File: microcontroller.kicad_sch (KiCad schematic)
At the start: 5 parts, among them CN4 Samtec FTSH-107-01-L-DV-K, CN5 M20-9990346, U2 TMP102AIDRL, U3 Microchip 24AA256UIDT-I/ST, U4 STM32H743VIT6

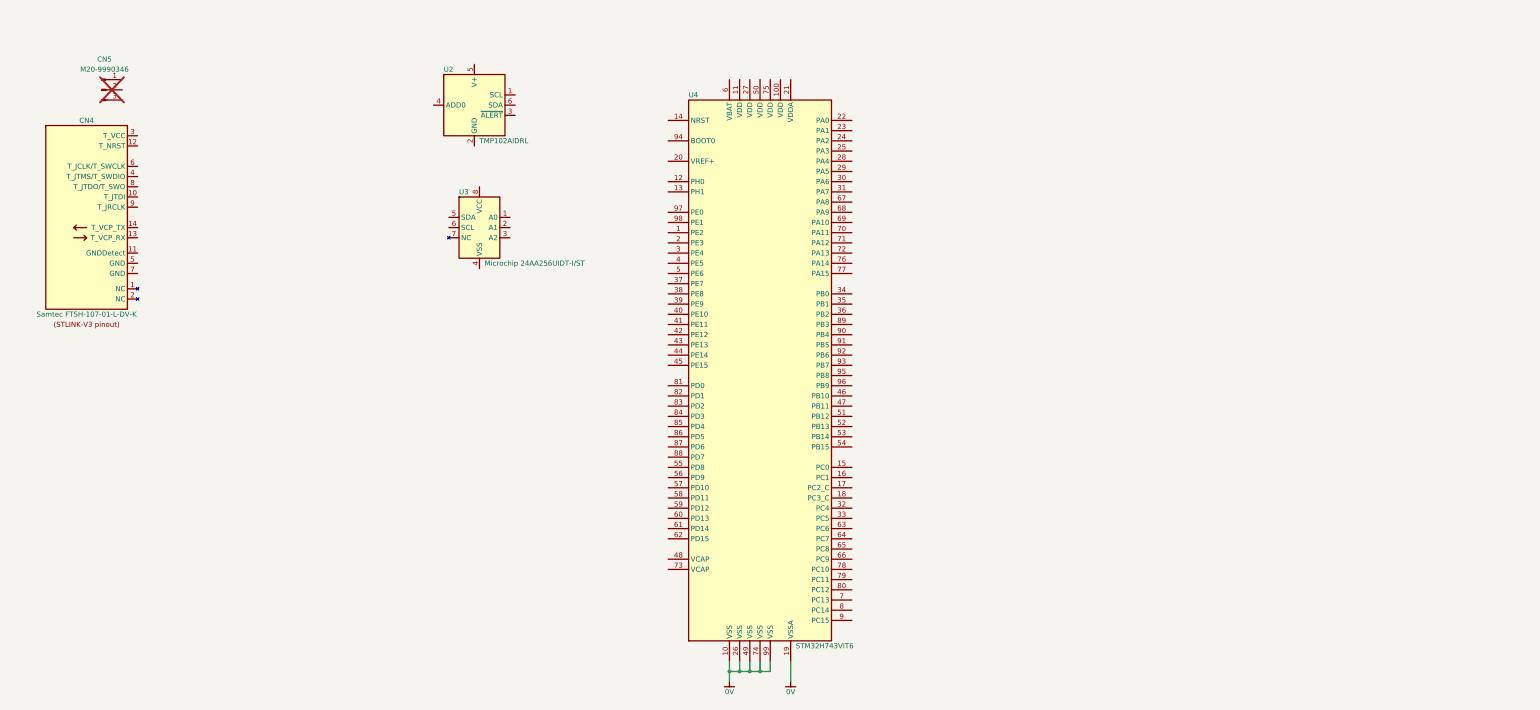
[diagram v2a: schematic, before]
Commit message: started on mcu pinout
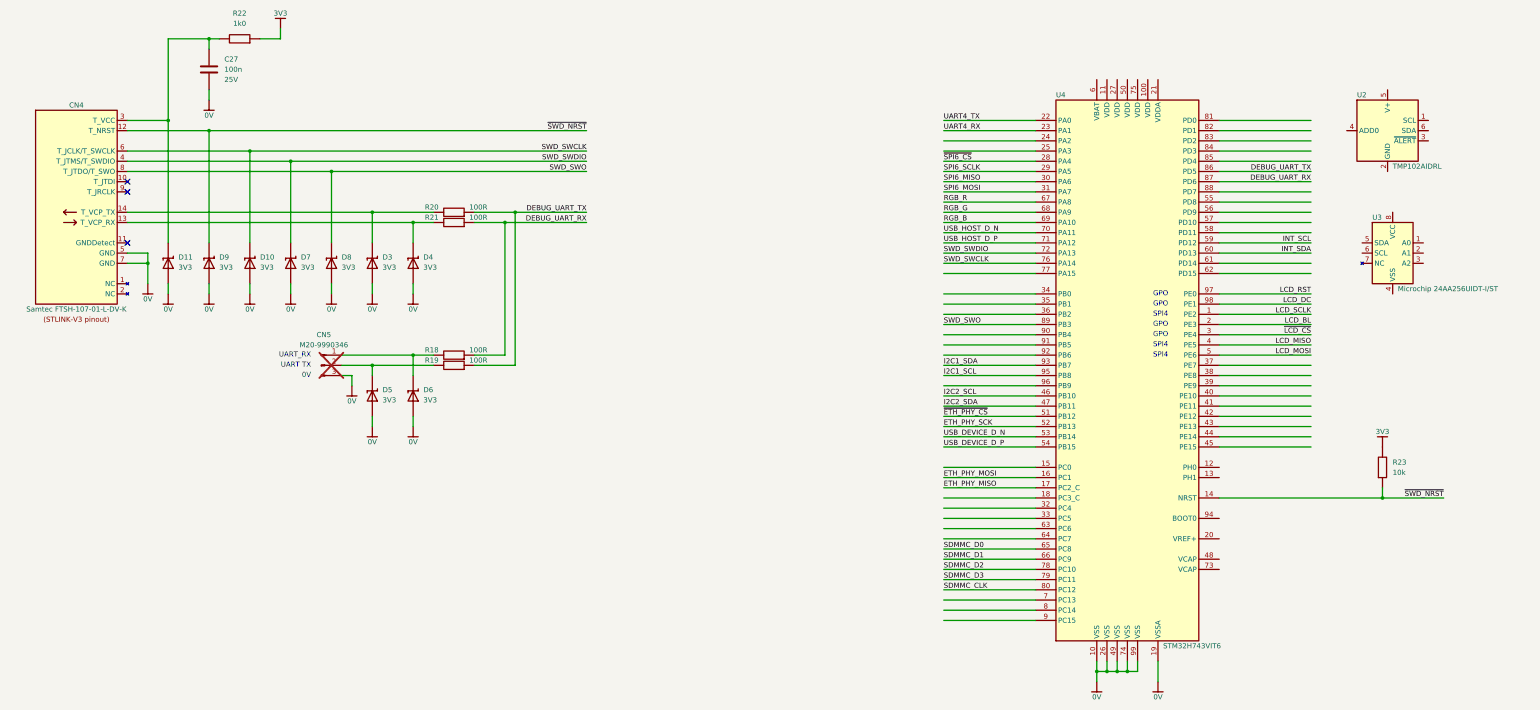
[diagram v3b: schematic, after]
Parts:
- added C27: 100n, Capacitor_WUT:C_0402_1005Metric, symbol aaa_capacitor_auto_wut:Yageo CC0402KRX7R8BB104
- added D10, D11, D3, D4, D5, D6, D7, D8, D9: 3V3, Diode_SMD:D_SOD-523, symbol aaa_tvs_zener_auto_wut:nexperia PESD3V3U1UB,115
- added R18, R19, R20, R21: 100R, Resistor_WUT:R_0402_1005Metric, symbol aaa_resistor_auto_wut:KOA Speer RK73H1ETTP1000F
- added R22: 1k0, Resistor_WUT:R_0402_1005Metric, symbol aaa_resistor_auto_wut:KOA Speer RK73H1ETTP1001F
- added R23: 10k, Resistor_WUT:R_0402_1005Metric, symbol aaa_resistor_auto_wut:KOA Speer RK73H1ETTP1002F
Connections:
- net 0V: now also CN4.5 (GND), CN4.7 (GND), CN5.3 (Pin_2), C27.2, D10.2 (A), D11.2 (A), D3.2 (A), D4.2 (A), D5.2 (A), D6.2 (A), D7.2 (A), D8.2 (A), D9.2 (A)
- net ~{SWD_NRST}: now reaches CN4.12 (T_NRST)
- net ~{SWD_NRST}: now also U4.14 (NRST), D9.1 (K), R23.2
- net at CN4.13 (T_VCP_RX): now also D4.1 (K), R21.1
- net at CN4.14 (T_VCP_TX): now also D3.1 (K), R20.1
- net at CN4.3 (T_VCC): now also C27.1, D11.1 (K), R22.1
- net SWD_SWDIO: now reaches CN4.4 (T_JTMS/T_SWDIO)
- net SWD_SWDIO: now also U4.72 (PA13), D7.1 (K)
- net SWD_SWCLK: now reaches CN4.6 (T_JCLK/T_SWCLK)
- net SWD_SWCLK: now also U4.76 (PA14), D10.1 (K)
- net SWD_SWO: now reaches CN4.8 (T_JTDO/T_SWO)
- net SWD_SWO: now also U4.89 (PB3), D8.1 (K)
- net at CN5.1 (Pin_1): now also D6.1 (K), R18.1
- net at CN5.2 (Pin_2): now also D5.1 (K), R19.1
- net LCD_SCLK: now reaches U4.1 (PE2)
- net ETH_PHY_MOSI: now reaches U4.16 (PC1)
- net ETH_PHY_MISO: now reaches U4.17 (PC2_C)
- net LCD_BL: now reaches U4.2 (PE3)
- net UART4_TX: now reaches U4.22 (PA0)
- net UART4_RX: now reaches U4.23 (PA1)
- net ~{SPI6_CS}: now reaches U4.28 (PA4)
- net SPI6_SCLK: now reaches U4.29 (PA5)
- net ~{LCD_CS}: now reaches U4.3 (PE4)
- net SPI6_MISO: now reaches U4.30 (PA6)
- net SPI6_MOSI: now reaches U4.31 (PA7)
- net LCD_MISO: now reaches U4.4 (PE5)
- net at U4.44 (PE14): no longer names the net of U4.44 (PE14)
- net I2C2_SCL: now reaches U4.46 (PB10)
- net I2C2_SDA: now reaches U4.47 (PB11)
- net LCD_MOSI: now reaches U4.5 (PE6)
- net ~{ETH_PHY_CS}: now reaches U4.51 (PB12)
- net ETH_PHY_SCK: now reaches U4.52 (PB13)
- net USB_DEVICE_D_N: now reaches U4.53 (PB14)
- net USB_DEVICE_D_P: now reaches U4.54 (PB15)
- net INT_SCL: now reaches U4.59 (PD12)
- net INT_SDA: now reaches U4.60 (PD13)
- net SDMMC_D0: now reaches U4.65 (PC8)
- net SDMMC_D1: now reaches U4.66 (PC9)
- net RGB_R: now reaches U4.67 (PA8)
- net RGB_G: now reaches U4.68 (PA9)
- net RGB_B: now reaches U4.69 (PA10)
- net USB_HOST_D_N: now reaches U4.70 (PA11)
- net USB_HOST_D_P: now reaches U4.71 (PA12)
- net SDMMC_D2: now reaches U4.78 (PC10)
- net SDMMC_D3: now reaches U4.79 (PC11)
- net SDMMC_CLK: now reaches U4.80 (PC12)
- net DEBUG_UART_TX: now reaches U4.86 (PD5)
- net DEBUG_UART_TX: now also R19.2, R20.2
- net DEBUG_UART_RX: now reaches U4.87 (PD6)
- net DEBUG_UART_RX: now also R18.2, R21.2
- net I2C1_SDA: now reaches U4.93 (PB7)
- net I2C1_SCL: now reaches U4.95 (PB8)
- net LCD_RST: now reaches U4.97 (PE0)
- net LCD_DC: now reaches U4.98 (PE1)
- new net 3V3: R22.2, R23.1
- no-connect marks 0 -> 3
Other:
- note added: "0V"
- note added: "GPO"
- note added: "SPI4"
- note added: "UART TX"
- note added: "UART_RX"
- moved on the sheet: CN4, CN5, U2, U3, U4

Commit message: more progress
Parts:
- added C16: 22u, Capacitor_SMD:C_0603_1608Metric, symbol aaa_capacitor_auto_wut:Murata GRM188R61C226ME01
- added C17: 4u7, Capacitor_WUT:C_0402_1005Metric, symbol capacitor_auto_wut:Murata GRM155D71A475ME15
- added C18, C19, C20, C21, C22, C23, C24, C28, C29: 100n, Capacitor_WUT:C_0402_1005Metric, symbol aaa_capacitor_auto_wut:Yageo CC0402KRX7R8BB104
- added C25, C26, C27: 2u2, Capacitor_WUT:C_0402_1005Metric, symbol capacitor_auto_wut:Murata GRM155R6YA225KE11
- added CN3: 104031-0811, Connector_WUT:microSD_HC_Molex_104031-0811, symbol Connector_WUT:Molex_104031-0811
- added CN5: Molex 105057-0001, Connector_WUT:USB-A_Molex_105057-0001_TH_Vertical, symbol Connector_WUT:Molex_105057-0001
- added D10: USBLC6-2P6, Package_TO_SOT_SMD:SOT-666, symbol Diode_WUT:ST_USBLC6-2P6
- added F1: 1A, Fuse:Fuse_0603_1608Metric, symbol fuse_auto_wut:Littelfuse 0467001.NR
- added FB3: 1k8, Inductor_SMD:L_0402_1005Metric, symbol aaa_ferrite_bead_auto_wut:Murata BLM15BD182SN1D
- added LD1: Wuerth 156125M173000, LED_WUT:Wuerth_156125M173000, symbol LED_WUT:Wuerth_156125M173000
- added R10: 10k, Resistor_WUT:R_0402_1005Metric, symbol aaa_resistor_auto_wut:KOA Speer RK73H1ETTP1002F
- added R23, R24, R25: 1k0, Resistor_WUT:R_0402_1005Metric, symbol aaa_resistor_auto_wut:KOA Speer RK73H1ETTP1001F
- added R26, R27, R28, R29, R30, R31: 33R, Resistor_WUT:R_0402_1005Metric, symbol aaa_resistor_auto_wut:KOA Speer RK73H1ETTP33R0F
- added ZF1: East Rising ER-TFTM019-1-SPI, Display_WUT:East-Rising_ER-TFTM019-1-SPI, symbol Display_WUT:East-Rising_ER-TFTM019-1-SPI
- renumbered C27 to C15, CN4 to CN2, CN5 to CN4, D11 to D1, D9 to D2, D10 to D3, D7 to D4, D8 to D5, D3 to D6, D5 to D7, D4 to D8, D6 to D9, R20 to R11, R21 to R12, R18 to R13, R19 to R14, R23 to R15, R22 to R9, U4 to U2, U2 to U3, U3 to U4
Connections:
- net 0V: now also C16.2, C17.2, C18.2, C19.2, C20.2, C21.2, C22.2, C23.2, C24.2, C25.2, C26.2, C27.2, C28.2, C29.2, CN3.11 (SHIELD), CN3.6 (VSS), CN3.9 (DET_B), CN5.4 (GND), D10.2 (GND)
- net 3V3: now also U2.100 (VDD), U2.11 (VDD), U2.27 (VDD), U2.50 (VDD), U2.6 (VBAT), U2.75 (VDD), C17.1, C18.1, C19.1, C20.1, C21.1, C22.1, C23.1, F1.2, FB3.2, LD1.4 (A), R10.1
- net LCD_BL: now also R31.1
- net LCD_DC: now also R29.1
- net LCD_MOSI: now also R27.1
- net LCD_RST: now also R28.1
- net LCD_SCLK: now also R26.1
- net RGB_B: now also U2.68 (PA9), R25.2; no longer U2.69 (PA10)
- net RGB_G: now also U2.67 (PA8), R24.2; no longer U2.68 (PA9)
- net RGB_R: now also U2.69 (PA10), R23.2; no longer U2.67 (PA8)
- net SDMMC_CLK: now also CN3.5 (CLK)
- net SDMMC_D0: now also CN3.7 (DAT0)
- net SDMMC_D1: now also CN3.8 (DAT1)
- net SDMMC_D2: now also CN3.1 (DAT2)
- net SDMMC_D3: now also CN3.2 (DAT3/CD)
- net USB_HOST_D_N: now also D10.4 (I/O2)
- net USB_HOST_D_P: now also D10.6 (I/O1)
- net ~{LCD_CS}: now also R30.1
- net ~{SWD_NRST}: now also C29.1
- net VDDA: now reaches U2.20 (VREF+)
- net VDDA: now also U2.21 (VDDA), C24.1, C26.1, C28.1, FB3.1
- net at U2.48 (VCAP): now also U2.73 (VCAP), C25.1, C27.1
- net USB_VBUS_EN: now reaches U2.61 (PD14)
- net ~{USB_VBUS_FAULT}: now reaches U2.62 (PD15)
- net ~{ETH_PHY_RESET}: now reaches U2.63 (PC6)
- net ~{ETH_PHY_INT}: now reaches U2.64 (PC7)
- net SDMMC_CMD: now reaches U2.83 (PD2)
- net SDMMC_CMD: now also CN3.3 (CMD)
- net ~{SD_CARD_DET}: now reaches U2.90 (PB4)
- net ~{SD_CARD_DET}: now also CN3.10 (DET_A), R10.2
- net ETH_PHY_MISO renamed MISO
- net ETH_PHY_MOSI renamed MOSI
- net ETH_PHY_SCK renamed SCLK
- net ~{ETH_PHY_CS} renamed ~{CS}
- new net: R28.2, ZF1.5 (RES)
- new net: LD1.1 (R), R23.1
- new net: R26.2, ZF1.3 (SCL)
- new net: R27.2, ZF1.4 (SDA)
- new net: R29.2, ZF1.6 (DC)
- new net: R30.2, ZF1.7 (~{CS})
- new net: R31.2, ZF1.8 (BLK)
- new net: LD1.3 (B), R25.1
- new net: LD1.2 (G), R24.1
- new net: C16.1, CN3.4 (VDD), F1.1
- new net: CN5.2 (D-), D10.3 (I/O2)
- new net: CN5.3 (D+), D10.1 (I/O1)
- new net 5V_VBUS: CN5.1 (VBUS), D10.5 (VBUS)
- no-connect marks 3 -> 4
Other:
- note added: "Figure 23 of datasheet"

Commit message: most things connected
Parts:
- added C45: 10u, Capacitor_SMD:C_0603_1608Metric, symbol aaa_capacitor_auto_wut:Samsung Electro-Mechanics CL10A106MO8NQNC
- added C46, C47, C48: 100n, Capacitor_WUT:C_0402_1005Metric, symbol aaa_capacitor_auto_wut:Yageo CC0402KRX7R8BB104
- added CN10, CN9: JST BM06B-SRSS-TB(LF)(SN), Connector_JST:JST_SH_BM06B-SRSS-TB_1x06-1MP_P1.00mm_Vertical, symbol Connector_WUT:Header_JST_BM06B-SRSS-TB(LF)(SN)
- added CN11: BM05B-SRSS-TB(LF)(SN), Connector_JST:JST_SH_BM05B-SRSS-TB_1x05-1MP_P1.00mm_Vertical, symbol Connector_WUT:Header_JST_BM05B-SRSS-TB(LF)(SN)
- added CN6: BM03B-SRSS-TB(LF)(SN), Connector_JST:JST_SH_BM03B-SRSS-TB_1x03-1MP_P1.00mm_Vertical, symbol Connector_WUT:Header_JST_BM03B-SRSS-TB(LF)(SN)
- added CN7, CN8: BM04B-SRSS-TB(LF)(SN), Connector_JST:JST_SH_BM04B-SRSS-TB_1x04-1MP_P1.00mm_Vertical, symbol Connector_WUT:Header_JST_BM04B-SRSS-TB(LF)(SN)
- added R35: 10k, Resistor_WUT:R_0402_1005Metric, symbol aaa_resistor_auto_wut:KOA Speer RK73H1ETTP1002F
- added R36, R37, R38, R39, R40, R41, R42, R43, R44, R45, R46, R47, R48, R49, R50, R51, R52, R53, R54, R55, R56, R57: 33R, Resistor_WUT:R_0402_1005Metric, symbol aaa_resistor_auto_wut:KOA Speer RK73H1ETTP33R0F
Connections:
- net 0V: now also CN5.5 (Shield), U3.2 (GND), U3.4 (ADD0), U4.1 (A0), U4.2 (A1), U4.3 (A2), U4.4 (VSS), ZF1.1 (GND), C45.2, C46.2, C47.2, C48.2, CN10.1 (Pin_1), CN11.1 (Pin_1), CN6.1 (Pin_1), CN7.1 (Pin_1), CN8.1 (Pin_1), CN9.1 (Pin_1), R35.2
- net 3V3: now also U3.5 (V+), U4.8 (VCC), ZF1.2 (VCC), C45.1, C47.1, C48.1
- net I2C1_SCL: now also U2.92 (PB6), R38.1; no longer U2.95 (PB8)
- net I2C1_SDA: now also R39.1
- net I2C2_SCL: now also R41.1
- net I2C2_SDA: now also R42.1
- net INT_SCL: now also U3.1 (SCL), U4.6 (SCL)
- net INT_SDA: now also U3.6 (SDA), U4.5 (SDA)
- net SPI6_MISO: now also R46.1
- net SPI6_MOSI: now also R47.1
- net SPI6_SCLK: now also R45.1
- net UART4_RX: now also R37.1
- net UART4_TX: now also R36.1
- net ~{CS}: now also U2.96 (PB9); no longer U2.51 (PB12)
- net ~{SD_CARD_DET}: now also U2.95 (PB8); no longer U2.90 (PB4)
- net ~{SPI6_CS}: now also R44.1
- net SPKR: now reaches U2.25 (PA3)
- net ~{INT_ALERT}: now reaches U2.58 (PD11)
- net ~{INT_ALERT}: now also U3.3 (~{ALERT})
- net ~{I2C1_ALERT}: now reaches U2.91 (PB5)
- net ~{I2C1_ALERT}: now also R40.1
- net DFU_EN: now reaches U2.94 (BOOT0)
- net DFU_EN: now also C46.1, R35.1
- new net: CN6.2 (Pin_2), R36.2
- new net: CN10.5 (Pin_2), R56.2
- new net: CN6.3 (Pin_2), R37.2
- new net: CN7.2 (Pin_2), R38.2
- new net: CN10.6 (Pin_2), R57.2
- new net: CN11.2 (Pin_2), R44.2
- new net: CN10.4 (Pin_2), R55.2
- new net: CN8.2 (Pin_2), R41.2
- new net: CN7.3 (Pin_2), R39.2
- new net: CN7.4 (Pin_2), R40.2
- new net: CN11.4 (Pin_2), R46.2
- new net: CN10.2 (Pin_2), R53.2
- new net: CN11.3 (Pin_2), R45.2
- new net: CN10.3 (Pin_2), R54.2
- new net: CN9.2 (Pin_2), R48.2
- new net: CN11.5 (Pin_2), R47.2
- new net: CN8.4 (Pin_2), R43.2
- new net: CN8.3 (Pin_2), R42.2
- new net: CN9.5 (Pin_2), R51.2
- new net: CN9.4 (Pin_2), R50.2
- new net: CN9.6 (Pin_2), R52.2
- new net: CN9.3 (Pin_2), R49.2
- new net ~{I2C2_ALERT}: R43.1, U2.51 (PB12)
- no-connect marks 4 -> 5
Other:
- note added: "Address = 0x48"
- note added: "Address = 0x50"
- note added: "I2C1"
- note added: "I2C2"
- note added: "I2C4"
- note added: "SDMMC1"
- note added: "SPI2"
- note added: "SPI6"
- note added: "SWD"
- note added: "TIM1_CH1"
- note added: "TIM1_CH2"
- note added: "TIM1_CH3"
- note added: "TIM2_CH4"
- note added: "UART4"
- note added: "USART2"
- note added: "USB only runs at FS with internal PHY"
- note added: "USB_OTG_FS"
- note added: "USB_OTG_HS"
- note added: "Using proper SMBus pin"
- moved on the sheet: C15, C16, C17, C18, C19, C20, C21, C22, C23, C24, C25, C26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
